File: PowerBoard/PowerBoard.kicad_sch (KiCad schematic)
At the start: 166 parts, among them IC101 LM340, IC102 7905, IC401 LM379, IC501 LM555xM, J103 Conn_01x02, J107 Conn_01x02, J204 Conn_01x04, J401 Conn_01x04, J402 Conn_01x04, J506 Conn_01x02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

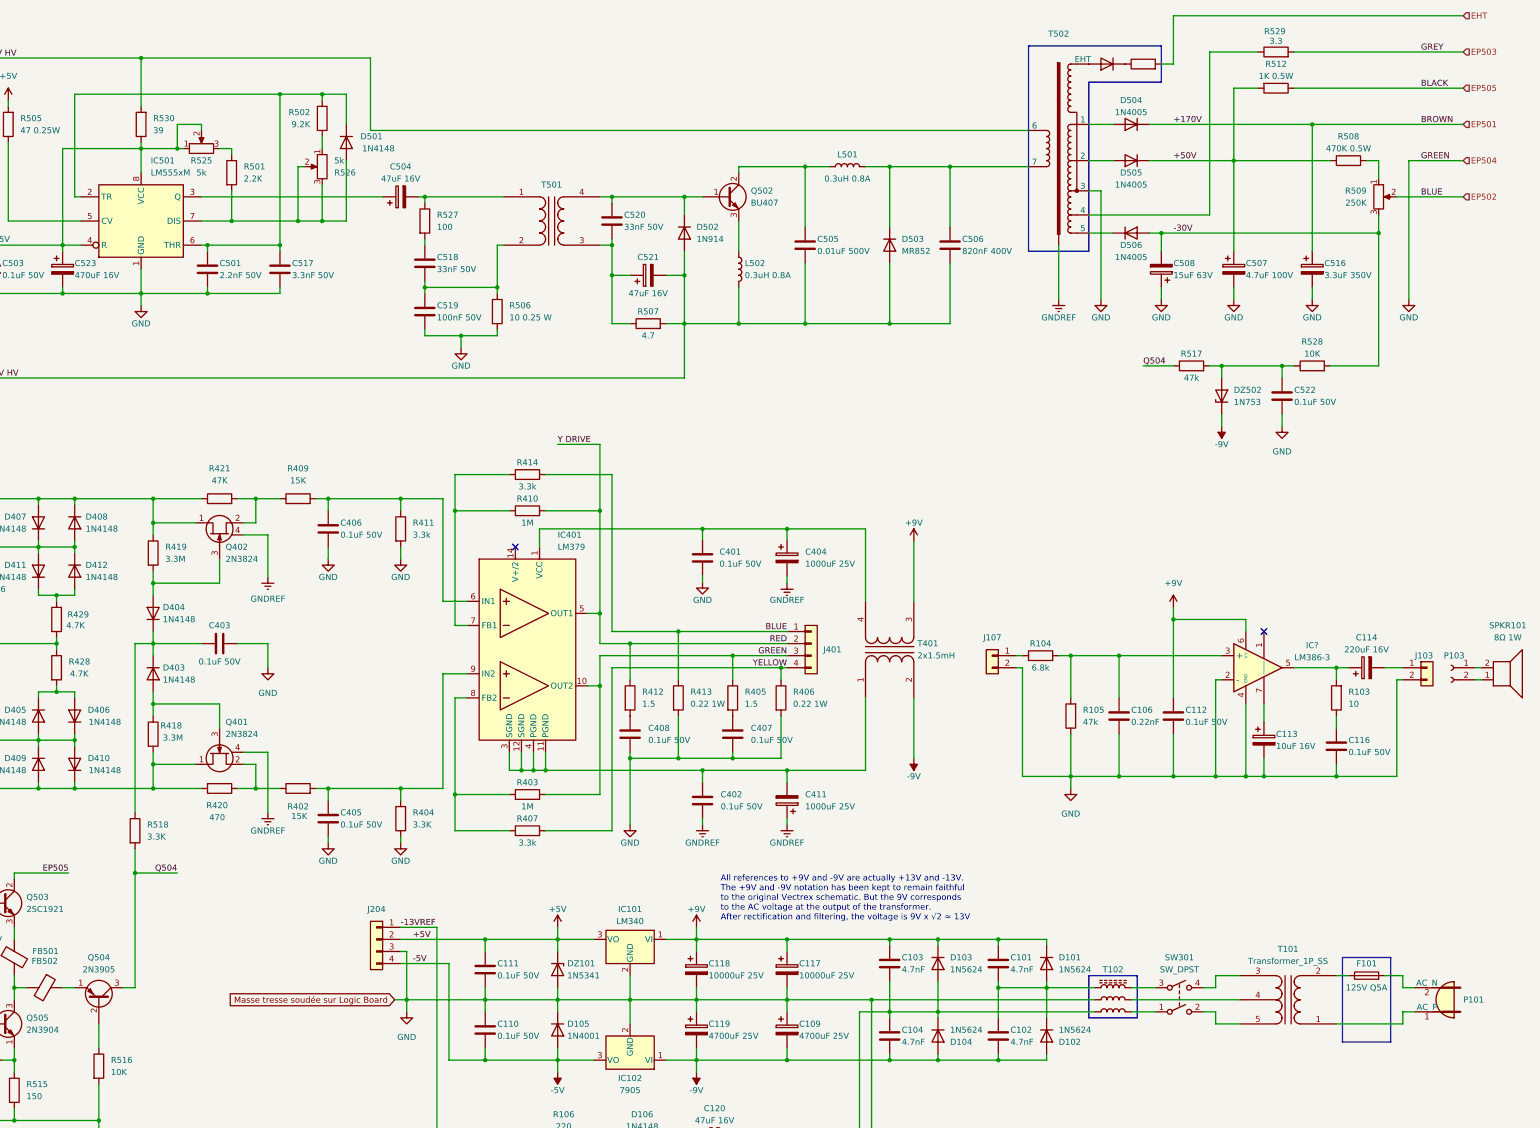
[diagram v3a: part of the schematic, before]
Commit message: correction to the LM379 on the PowerBoard
- Convert to Kicad 8
- Correction to the LM379 on the PowerBoard and C405,C406,R404,R411
- Correct value of F101
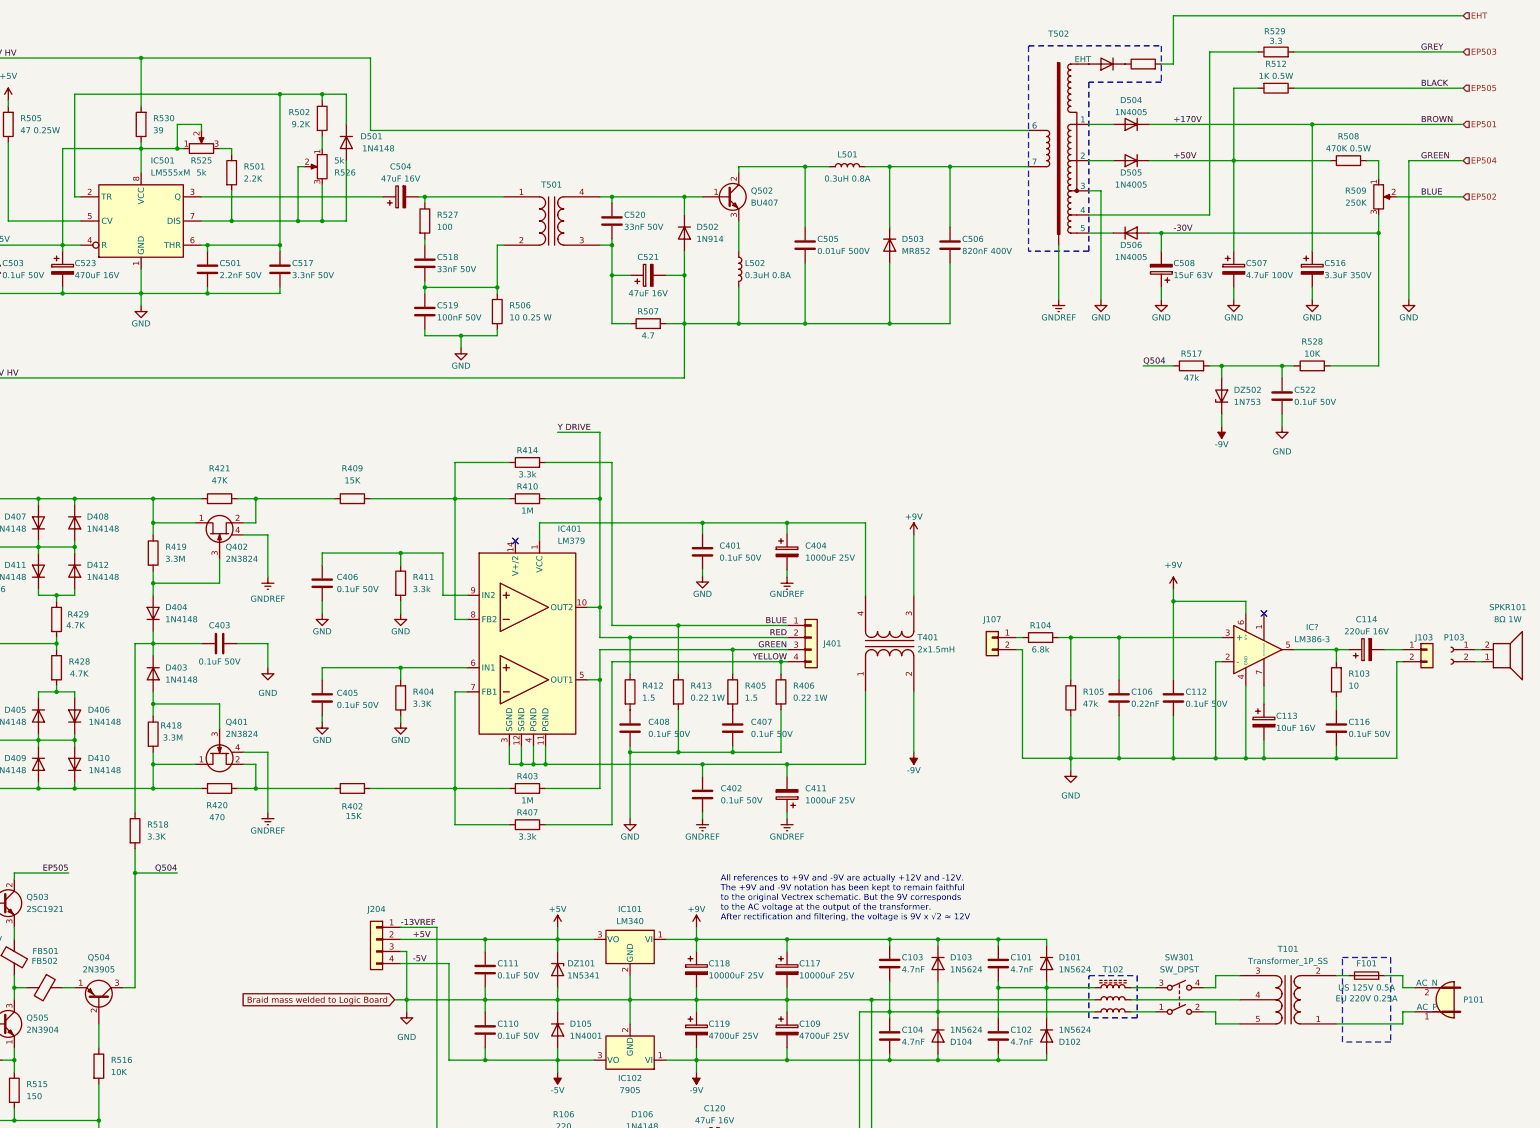
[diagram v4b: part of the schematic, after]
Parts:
- C506: value 820nF 400V -> 820nF 400V
- D101, D102, D103, D104, D105, D106, D107, D401, D402, D403, D404, D405, D406, D407, D408, D409, D410, D411, D412, D503: Spice_Netlist_Enabled Y -> (none); Spice_Primitive D -> (none)
- D?: value DIODE -> ${SIM.PARAMS}; Spice_Netlist_Enabled Y -> (none); Spice_Primitive D -> (none)
- F101: value 125V Q5A -> US 125V 0.5A; Valeur EU (none) -> EU 220V 0.25A
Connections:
- net GND: now also IC401.5 (OUT1); no longer IC401.10 (OUT2)
- net RED: now also IC401.10 (OUT2); no longer IC401.5 (OUT1)
- net at C406.2, R411.1: now also IC401.9 (IN2); no longer IC401.6 (IN1), R409.2
- net at R410.1, R414.1: now also IC401.8 (FB2), R409.2; no longer IC401.7 (FB1)
- net at C405.2, R404.2: now also IC401.6 (IN1); no longer IC401.9 (IN2), R402.2
- net at R403.1, R407.1: now also IC401.7 (FB1), R402.2; no longer IC401.8 (FB2)
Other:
- note added: "All references to +9V and -9V are actually +12V and -12V. The +9V and -9V notation has been kept to remain faithful to the original Vectrex schematic. But the 9V corresponds to the AC voltage at the output of the transformer. After rectification and filtering, the voltage is 9V x √2 ≈ 12V"
- note removed: "All references to +9V and -9V are actually +13V and -13V. The +9V and -9V notation has been kept to remain faithful to the original Vectrex schematic. But the 9V corresponds to the AC voltage at the output of the transformer. After rectification and filtering, the voltage is 9V x √2 ≈ 13V"
- moved on the sheet: C106, C112, C113, C114, C116, C401, C402, C404, C405, C406, C407, C408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
